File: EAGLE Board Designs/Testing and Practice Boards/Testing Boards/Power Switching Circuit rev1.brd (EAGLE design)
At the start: 93.4 x 66.3 mm, 47 parts, among them K1 J115F11A6*, Q1 SIR638ADP, Q2 SIR638ADP, Q3 SIR638ADP, Q4 SIR638ADP, U1 LTC4421, X1 CONNECTOR-4AUTOSPORT, X2 CONNECTOR-4AUTOSPORT, X3 CONNECTOR-3

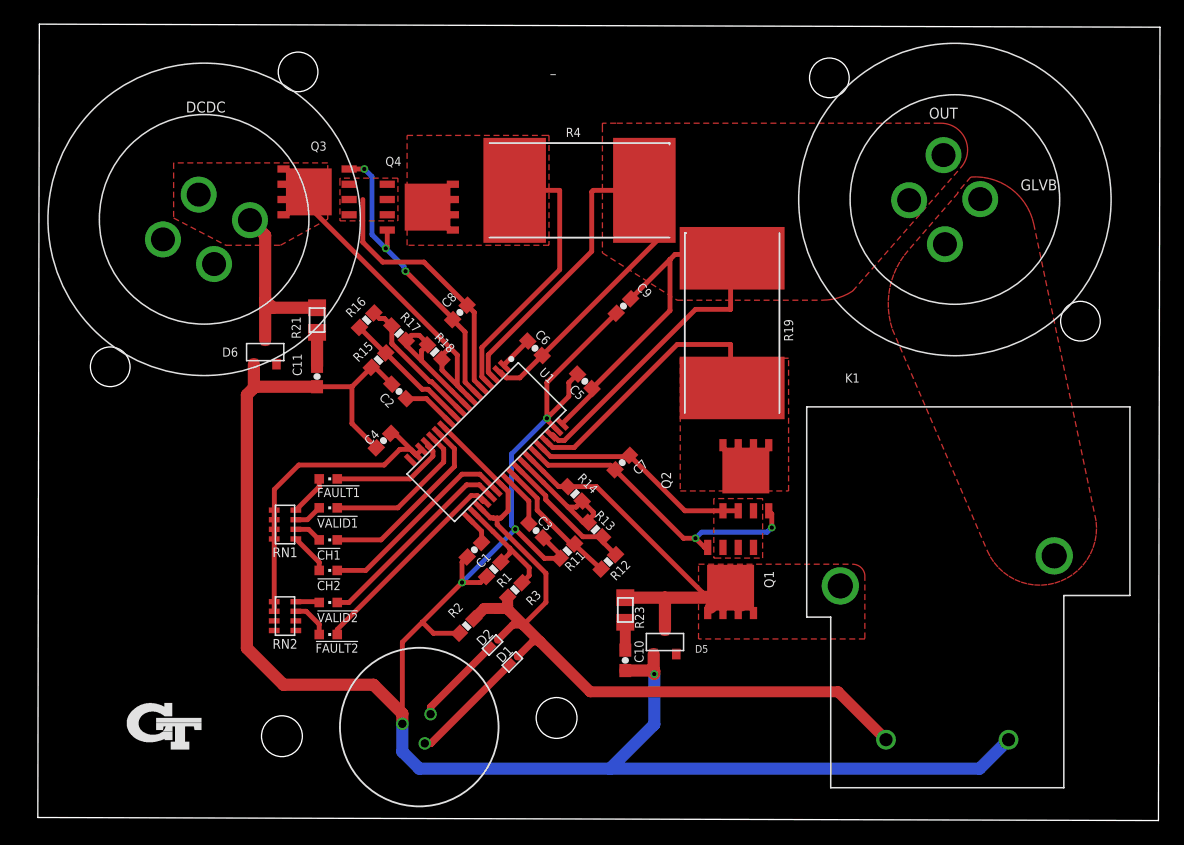
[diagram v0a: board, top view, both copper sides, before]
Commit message: Added mount holes and made minor polygon changes
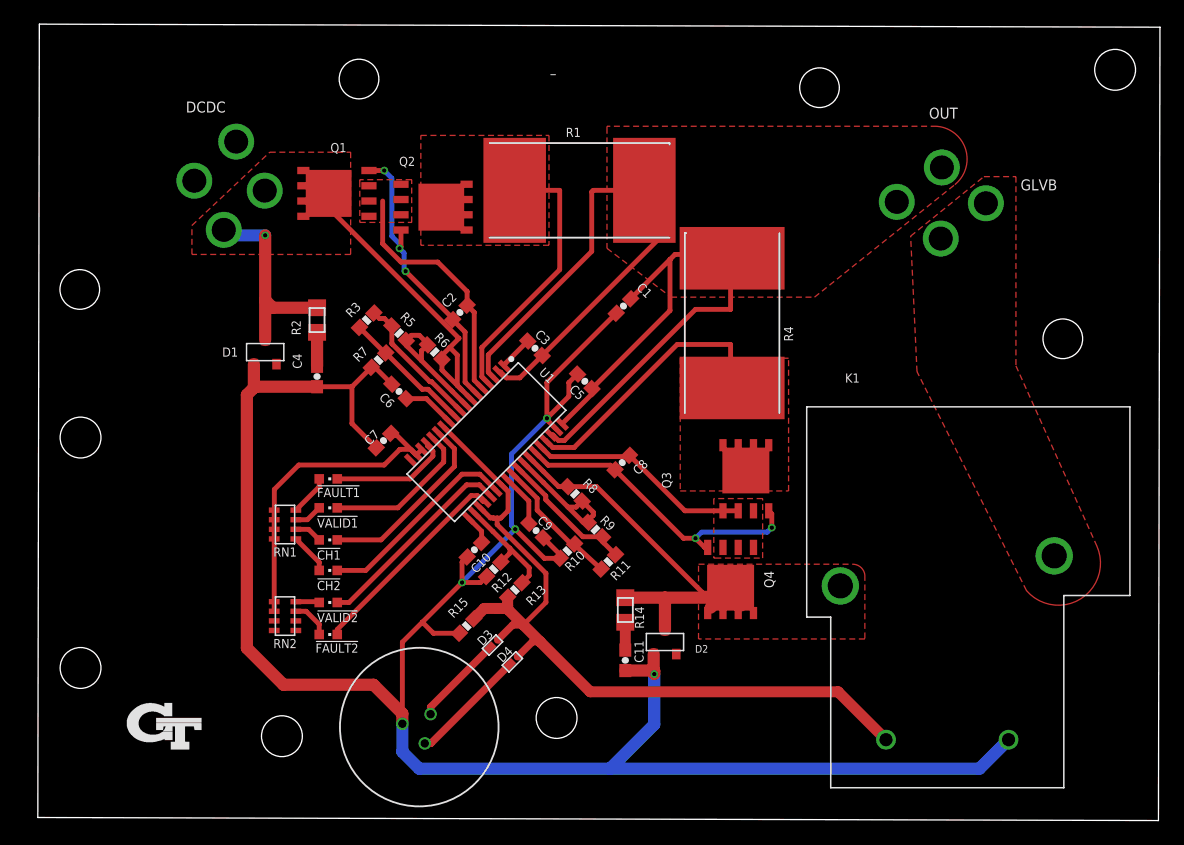
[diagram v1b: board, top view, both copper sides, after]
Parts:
- removed D5, D6: TVS_15V, HyTechDevices:SOT-23
- removed R16: 11k, HyTechDevices:0603-RES
- removed R19: 0.001, HyTechDevices:5930-SENSE_RES
- removed R21: 0.55, HyTechDevices:0805
- removed R23: 0.65, HyTechDevices:0805
- removed X2: CONNECTOR-4AUTOSPORT, HyTechDevices:AUTOSPORT_12-04
- removed X3: CONNECTOR-3, HyTechDevices:AUTOSPORT_04-35
- added D3, D4: SCHOTTKY, HyTechDevices:CLP1608-2L
- added R10: 31k, HyTechDevices:0603-RES
- added R7: 35k, HyTechDevices:0603-RES
- added R8: 950k, HyTechDevices:0603-RES
- added R9: 9.5k, HyTechDevices:0603-RES
- added U$1, U$3, U$4: (no value), HyTechDevices:MOUNTING_M3
- added X100, X101: CONNECTOR-4AUTOSPORT, HyTechDevices:AUTOSPORT_12-04
- C1: value 1nF -> 600uF
- C10: value 10uF -> 1nF
- C2: value 6.8nF -> 47nF
- C3: value 6.8nF -> 1uF
- C4: value 1uF -> 10uF
- C6: value 1uF -> 6.8nF
- C7: value 47nF -> 1uF
- C9: value 600uF -> 6.8nF
- D1, D2: value SCHOTTKY -> TVS_15V; device HyTechDevices:CLP1608-2L -> HyTechDevices:SOT-23
- LED1: value GREEN -> RED
- LED5: value RED -> GREEN
- R1: value 0 -> 0.001; device HyTechDevices:0603-RES -> HyTechDevices:5930-SENSE_RES
- R11: value 31k -> 19k
- R12: value 19k -> 0
- R13: value 9.5k -> 0
- R14: value 950k -> 0.65; device HyTechDevices:0603-RES -> HyTechDevices:0805
- R15: value 35k -> 10k
- R2: value 10k -> 0.55; device HyTechDevices:0603-RES -> HyTechDevices:0805
- R3: value 0 -> 11k
- X1: value CONNECTOR-4AUTOSPORT -> CONNECTOR-3; device HyTechDevices:AUTOSPORT_12-04 -> HyTechDevices:AUTOSPORT_04-35
- moved X1 63.0 mm to (3.43, -19.3), turned to 138.8 degrees
- moved Q1 45.7 mm to (-3.05, 25.3), turned to 180 degrees
- moved Q3 42.7 mm to (30.7, 1.52), turned to 90 degrees
- moved Q4 40.6 mm to (29.7, -6.60), turned to 270 degrees
- moved C11 34.9 mm to (20.8, -13.5)
- moved Q2 34.6 mm to (4.70, 24.4), turned to 0 degrees
- moved D1 33.0 mm to (-9.14, 12.2), turned to 0 degrees
- moved R1 32.3 mm to (17.0, 25.7), turned to 0 degrees
- moved R2 28.3 mm to (-4.83, 14.9), turned to 90 degrees
- moved R3 25.6 mm to (-0.70, 14.8)
- moved C1 23.8 mm to (20.7, 16.0)
- moved R15 23.3 mm to (7.62, -10.6)
- moved C9 20.1 mm to (13.4, -2.66), turned to 315 degrees
- moved C7 20.0 mm to (0.70, 4.83)
- moved C8 18.4 mm to (20.6, 3.00)
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- renumbered R17 to R5, R18 to R6
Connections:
- removed net GLVMS: D2.1, X3.B
- new net RIGHT_BRB: D3.1, X1.B
- net !FAULT1: now also LED1.C; no longer LED5.C
- net !SHDN: now also D3.2, D4.2, R13.1, R15.2; no longer D1.2, D2.2, R2.2, R3.1
- net !VALID1: now also LED2.C; no longer LED1.C
- net !VALID2: now also LED5.C; no longer LED2.C
- net CASIN: now also C7.1; no longer C4.1
- net CPO: now also C3.2; no longer C6.2
- net DCDC: now also D1.3, Q1.D@5, Q1.D@6, Q1.D@7, Q1.D@8, Q1.D@PAD, R2.2, X101.1, X101.4; no longer D6.3, Q3.D@5, Q3.D@6, Q3.D@7, Q3.D@8, Q3.D@PAD, R21.2, X2.3, X2.4
- net GATE1: now also C2.2, Q1.4, Q2.4; no longer C8.2, Q3.4, Q4.4
- net GATE2: now also C8.2, Q3.4, Q4.4; no longer C7.2, Q1.4, Q2.4
- net GLVB: now also X100.3, X100.4; no longer X1.3, X1.4
- net GND: now also C6.2, C7.2, D1.1, D2.1, R10.1, R12.2, R7.1, X1.A; no longer C2.2, C3.2, D5.1, D6.1, R1.2, R11.1, R2.1, X3.A
- net N$1: now also C10.1; no longer C1.1
- net N$13: now also LED1.A; no longer LED5.A
- net N$19: now also LED5.A; no longer LED2.A
- net N$2: now also C6.1; no longer C2.1
- net N$21: now also LED2.A; no longer LED1.A
- net N$22: now also C4.1, R2.1; no longer C11.1, R21.1
- net N$3: now also C9.1; no longer C3.1
- net N$4: now also C11.1, R14.1; no longer C10.1, R23.1
- net OUT: now also C1.1, C3.1, R1.2, X100.1, X100.2; no longer C6.1, C9.1, R19.2, X1.1, X1.2
- net OV1: now also R3.1, R7.2; no longer R15.2, R16.1
- net OV2: now also R10.2, R11.1; no longer R11.2, R12.1
- net RELAY: now also D2.3, Q4.D@5, Q4.D@6, Q4.D@7, Q4.D@8, Q4.D@PAD, R8.2; no longer D5.3, Q1.D@5, Q1.D@6, Q1.D@7, Q1.D@8, Q1.D@PAD, R23.2
- net RETRY: now also R12.1, R13.2; no longer R1.1, R3.2
- net SENSE: now also Q2.D@5, Q2.D@6, Q2.D@7, Q2.D@8, Q2.D@PAD, R1.1; no longer Q4.D@5, Q4.D@6, Q4.D@7, Q4.D@8, Q4.D@PAD, R4.1
- net SENSE2: now also Q3.D@5, Q3.D@6, Q3.D@7, Q3.D@8, Q3.D@PAD, R4.1; no longer Q2.D@5, Q2.D@6, Q2.D@7, Q2.D@8, Q2.D@PAD, R19.1
- net SOURCE1: now also C2.1, Q1.1, Q1.2, Q1.3, Q2.1, Q2.2, Q2.3; no longer C8.1, Q3.1, Q3.2, Q3.3, Q4.1, Q4.2, Q4.3
- net SOURCE2: now also C8.1, Q3.1, Q3.2, Q3.3, Q4.1, Q4.2, Q4.3; no longer C7.1, Q1.1, Q1.2, Q1.3, Q2.1, Q2.2, Q2.3
- net START: now also D4.1, X1.C; no longer D1.1, X3.C
- net UVF2: now also R8.1, R9.2; no longer R13.2, R14.1
- net UVR1: now also R3.2; no longer R16.2
- net UVR2: now also R11.2, R9.1; no longer R12.2, R13.1
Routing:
- net RIGHT_BRB: track 0.00 -> 7.59 mm
- net GLVMS: track 7.59 -> 0.00 mm
- net DCDC: track 42.5 -> 44.3 mm, vias 0 -> 1
- net SOURCE1: track 21.9 -> 20.8 mm
- net GATE1: track 25.5 -> 24.7 mm

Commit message: Minor fixes
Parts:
- moved U$4 0.40 mm to (61.7, 36.1)
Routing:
- net DCDC: track 44.3 -> 43.7 mm
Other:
- board size 93.4 x 66.3 mm -> 93.2 x 66.3 mm
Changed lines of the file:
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@@
 <drawing>
 <settings>
-<setting alwaysvectorfont="yes"/>
+<setting alwaysvectorfont="no"/>
 <setting verticaltext="up"/>
 </settings>
@@
 <layer number="17" name="Pads" color="2" fill="1" visible="yes" active="yes"/>
 <layer number="18" name="Vias" color="2" fill="1" visible="yes" active="yes"/>
-<layer number="19" name="Unrouted" color="6" fill="1" visible="no" active="yes"/>
+<layer number="19" name="Unrouted" color="6" fill="1" visible="yes" active="yes"/>
 <layer number="20" name="Dimension" color="24" fill="1" visible="yes" active="yes"/>
 <layer number="21" name="tPlace" color="7" fill="1" visible="yes" active="yes"/>
@@
 <layer number="26" name="bNames" color="7" fill="1" visible="yes" active="yes"/>
 <layer number="27" name="tValues" color="7" fill="1" visible="yes" active="yes"/>
-<layer number="28" name="bValues" color="7" fill="1" visible="no" active="yes"/>
-<layer number="29" name="tStop" color="7" fill="3" visible="yes" active="yes"/>
-<layer number="30" name="bStop" color="7" fill="6" visible="yes" active="yes"/>
-<layer number="31" name="tCream" color="7" fill="4" visible="yes" active="yes"/>
+<layer number="28" name="bValues" color="7" fill="1" visible="yes" active="yes"/>
+<layer number="29" name="tStop" color="7" fill="3" visible="no" active="yes"/>
+<layer number="30" name="bStop" color="7" fill="6" visible="no" active="yes"/>
+<layer number="31" name="tCream" color="7" fill="4" visible="no" active="yes"/>
 <layer number="32" name="bCream" color="7" fill="5" visible="no" active="yes"/>
 <layer number="33" name="tFinish" color="6" fill="3" visible="no" active="yes"/>
 <layer number="34" name="bFinish" color="6" fill="6" visible="no" active="yes"/>
-<layer number="35" name="tGlue" color="7" fill="4" visible="yes" active="yes"/>
+<layer number="35" name="tGlue" color="7" fill="4" visible="no" active="yes"/>
 <layer number="36" name="bGlue" color="7" fill="5" visible="no" active="yes"/>
 <layer number="37" name="tTest" color="7" fill="1" visible="no" active="yes"/>
@@
 <layer number="39" name="tKeepout" color="4" fill="11" visible="yes" active="yes"/>
 <layer number="40" name="bKeepout" color="1" fill="11" visible="yes" active="yes"/>
-<layer number="41" name="tRestrict" color="4" fill="10" visible="yes" active="yes"/>
-<layer number="42" name="bRestrict" color="1" fill="10" visible="yes" active="yes"/>
+<layer number="41" name="tRestrict" color="4" fill="10" visible="no" active="yes"/>
+<layer number="42" name="bRestrict" color="1" fill="10" visible="no" active="yes"/>
 <layer number="43" name="vRestrict" color="2" fill="10" visible="no" active="yes"/>
-<layer number="44" name="Drills" color="7" fill="1" visible="yes" active="yes"/>
-<layer number="45" name="Holes" color="7" fill="1" visible="yes" active="yes"/>
+<layer number="44" name="Drills" color="7" fill="1" visible="no" active="yes"/>
+<layer number="45" name="Holes" color="7" fill="1" visible="no" active="yes"/>
 <layer number="46" name="Milling" color="3" fill="1" visible="no" active="yes"/>
 <layer number="47" name="Measures" color="7" fill="1" visible="no" active="yes"/>
@@
 <layer number="50" name="dxf" color="7" fill="1" visible="no" active="no"/>
 <layer number="51" name="tDocu" color="7" fill="1" visible="yes" active="yes"/>
-<layer number="52" name="bDocu" color="7" fill="1" visible="no" active="yes"/>
+<layer number="52" name="bDocu" color="7" fill="1" visible="yes" active="yes"/>
 <layer number="53" name="tGND_GNDA" color="7" fill="9" visible="no" active="no"/>
 <layer number="54" name="bGND_GNDA" color="1" fill="9" visible="no" active="no"/>
@@
 <board>
 <plain>
-<wire x1="-28.067" y1="-26.543" x2="65.202" y2="-26.797" width="0" layer="20"/>
-<wire x1="65.202" y1="-26.797" x2="65.329" y2="39.233" width="0" layer="20"/>
-<wire x1="65.329" y1="39.233" x2="-27.94" y2="39.487" width="0" layer="20"/>
-<wire x1="-27.94" y1="39.487" x2="-28.067" y2="-26.543" width="0" layer="20"/>
+<wire x1="-28.067" y1="-26.543" x2="65.151" y2="-26.797" width="0" layer="20"/>
+<wire x1="65.151" y1="-26.797" x2="65.151" y2="39.497" width="0" layer="20"/>
+<wire x1="65.151" y1="39.497" x2="-27.94" y2="39.497" width="0" layer="20"/>
+<wire x1="-27.94" y1="39.497" x2="-28.067" y2="-26.543" width="0" layer="20"/>
 <text x="-4.953" y="-12.827" size="0.762" layer="21" font="vector">!FAULT2</text>
 <text x="-4.826" y="0.127" size="0.762" layer="21" font="vector">!FAULT1</text>
@@
 <element name="U$1" library="HyTechDevices" package="MOUNTING_M3" value="" x="-24.511" y="-14.097" smashed="yes"/>
 <element name="U$3" library="HyTechDevices" package="MOUNTING_M3" value="" x="-24.511" y="5.08" smashed="yes"/>
-<element name="U$4" library="HyTechDevices" package="MOUNTING_M3" value="" x="61.595" y="35.687" smashed="yes"/>
+<element name="U$4" library="HyTechDevices" package="MOUNTING_M3" value="" x="61.722" y="36.068" smashed="yes"/>
 </elements>
 <signals>
@@
 <wire x1="5.56790625" y1="11.595146875" x2="5.56790625" y2="11.91790625" width="0.4064" layer="1"/>
 <wire x1="5.56790625" y1="11.91790625" x2="6.223" y2="12.573" width="0.4064" layer="1"/>
-<wire x1="6.223" y1="12.573" x2="6.985" y2="13.335" width="0.4064" layer="1"/>
-<wire x1="-3.8608" y1="25.4" x2="-3.8608" y2="24.1808" width="0.4064" layer="1"/>
-<wire x1="-3.8608" y1="24.1808" x2="6.985" y2="13.335" width="0.4064" layer="1"/>
+<wire x1="-3.8608" y1="25.4" x2="-3.8608" y2="22.6568" width="0.4064" layer="1"/>
+<wire x1="-3.8608" y1="22.6568" x2="6.223" y2="12.573" width="0.4064" layer="1"/>
 <wire x1="-9.144" y1="16.51" x2="-9.144" y2="13.1953" width="1.016" layer="1"/>
 <via x="-9.144" y="21.908628125" extent="1-16" drill="0.35"/>
@@
 <vertex x="-1.27" y="22.987"/>
 <vertex x="3.048" y="22.987"/>
-<vertex x="3.048" y="22.987"/>
 <vertex x="3.048" y="26.543"/>
 <vertex x="-1.27" y="26.543"/>
@@
 <wire x1="7.6626375" y1="16.09439375" x2="7.6626375" y2="17.23739375" width="0.4064" layer="1"/>
 <wire x1="7.6626375" y1="17.23739375" x2="5.21503125" y2="19.685" width="0.4064" layer="1"/>
-<wire x1="5.21503125" y1="19.685" x2="2.159" y2="19.685" width="0.4064" layer="1"/>
-<wire x1="2.159" y1="19.685" x2="0.635" y2="21.209" width="0.4064" layer="1"/>
-<wire x1="0.635" y1="21.209" x2="0.635" y2="24.765" width="0.4064" layer="1"/>
+<wire x1="5.21503125" y1="19.685" x2="1.905" y2="19.685" width="0.4064" layer="1"/>
+<wire x1="1.905" y1="19.685" x2="0.635" y2="20.955" width="0.4064" layer="1"/>
+<wire x1="0.635" y1="20.955" x2="0.635" y2="24.765" width="0.4064" layer="1"/>
 </signal>
 <signal name="!SHDN">
